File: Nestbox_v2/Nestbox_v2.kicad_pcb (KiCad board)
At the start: 2 copper layers, 85 x 60 mm, 108 parts, among them CON301 Micro_SD_Card, J201 BATT_CONN_01X02, J401 LB_DETECT_CONN_01X04, J402 CONN_01X05, J501 CONN_01X01, J502 CONN_01X06, J601 LOAD_CELL_CONN_01X04, J701 RFID_CONN_01X05, P301 RX/TX, P302 TST/RST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

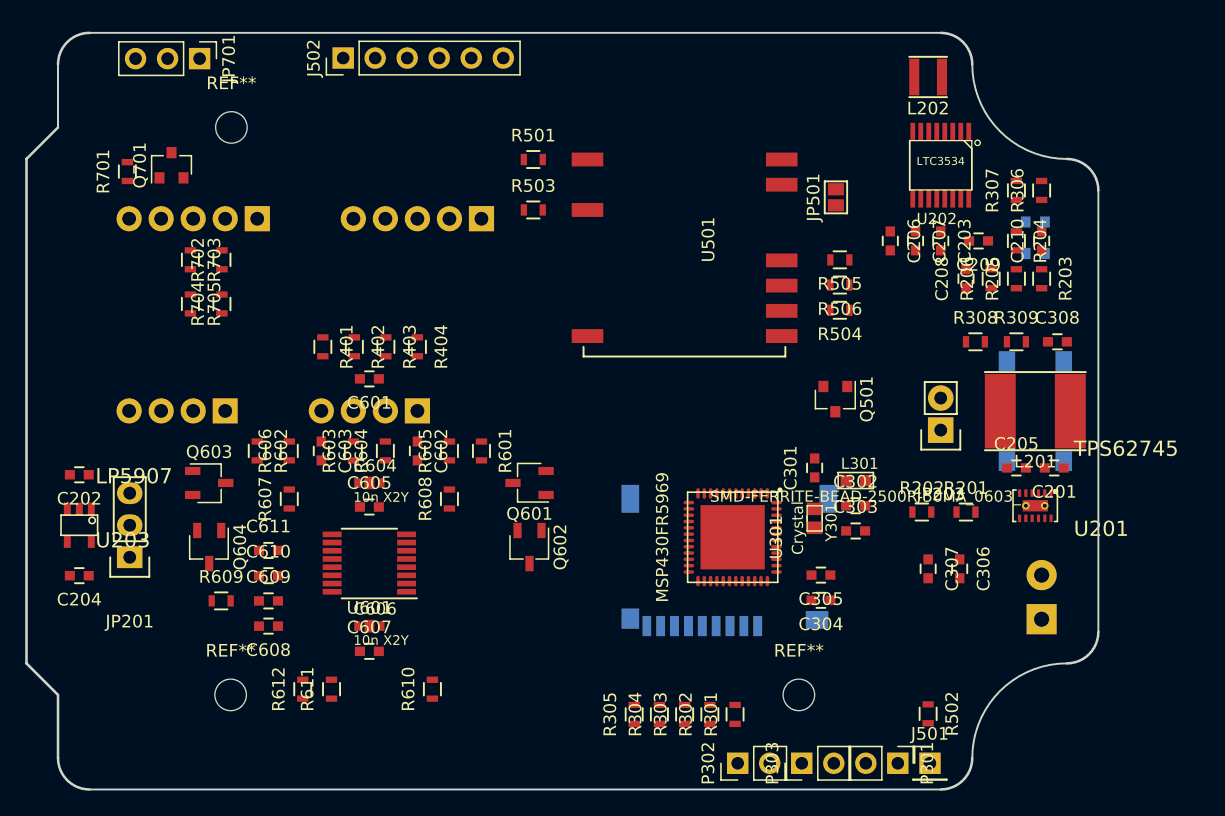
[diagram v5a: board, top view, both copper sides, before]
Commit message: routed all tracks except ground plane
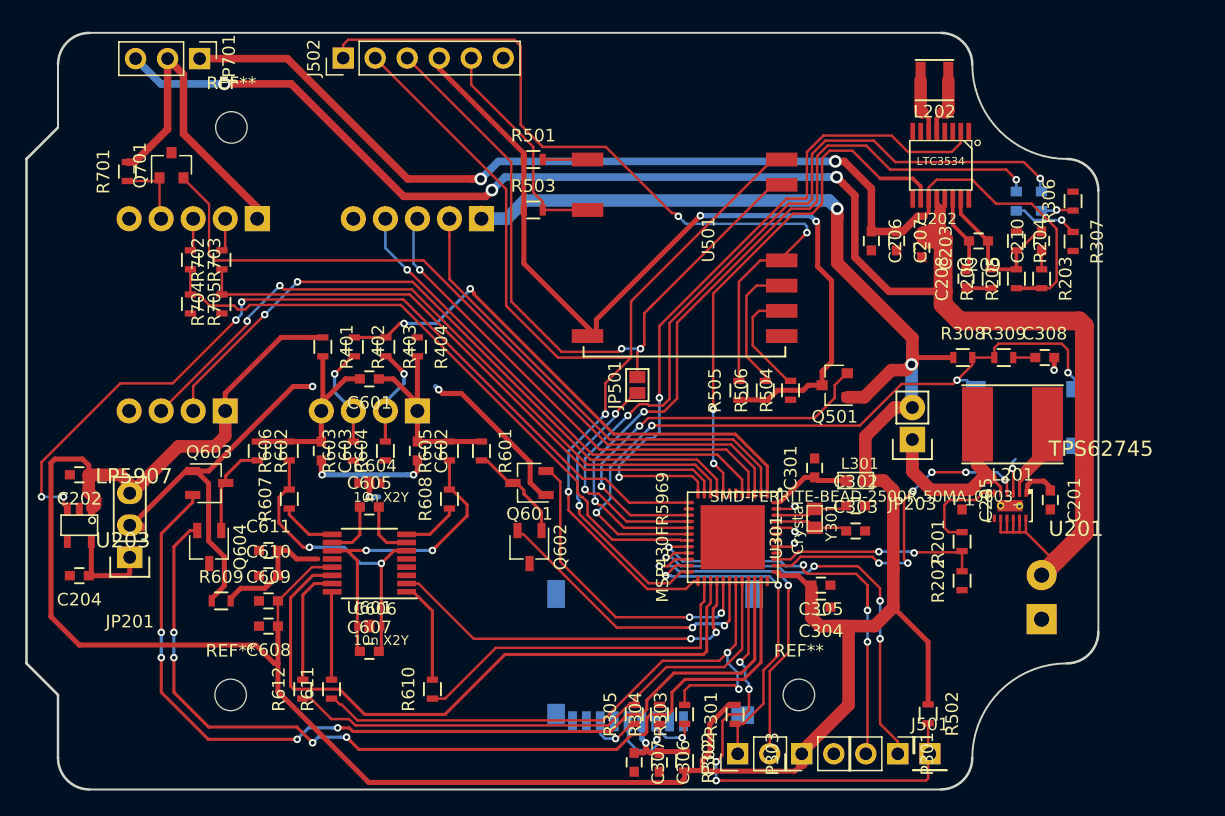
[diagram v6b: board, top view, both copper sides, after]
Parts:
- moved C306 28.3 mm to (82.7, 185.3)
- moved C307 27.9 mm to (80.7, 185.3)
- moved JP501 21.7 mm to (80.9, 155.4)
- moved R505 13.1 mm to (89.0, 155.9), turned to 90 degrees
- moved R506 10.2 mm to (91.1, 155.9), turned to 90 degrees
- moved CON301 9.58 mm to (82.3, 182.1)
- moved R504 7.45 mm to (93.1, 155.8), turned to 90 degrees
- moved R202 6.31 mm to (106.7, 170.9), turned to 90 degrees
- moved R307 6.04 mm to (115.5, 144.0), turned to 270 degrees
- moved C205 5.01 mm to (106.7, 164.5), turned to 270 degrees
- moved D302 4.42 mm to (111.0, 140.8), turned to 270 degrees
- moved R302 4.21 mm to (84.7, 185.2), turned to 270 degrees
- moved R306 2.63 mm to (115.5, 140.8)
- moved C201 2.56 mm to (113.7, 164.5), turned to 270 degrees
- moved JP203 2.37 mm to (102.8, 159.8)
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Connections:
- U201 pad 2: (no net) -> Net-(L201-Pad1)
- U201 pad 3: Net-(L201-Pad1) -> GND
- U301 pad 11: (no net) -> /Control/RFID_CLK
- U301 pad 14: /Control/BAT_TEST_ENABLE -> (no net)
- U301 pad 38: /PIR_OUT1 -> /Control/BAT_TEST_ENABLE
- U301 pad 39: /PIR_OUT2 -> /Control/HK_BAT_V
- U301 pad 4: (no net) -> /PIR_OUT1
- U301 pad 40: /Control/RFID_CLK -> (no net)
- U301 pad 5: (no net) -> /PIR_OUT2
- U301 pad 6: /Control/HK_BAT_V -> (no net)
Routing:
- net +3V3: track 0.00 -> 246.2 mm, vias 0 -> 2
- net +BATT: track 0.00 -> 144.1 mm, vias 0 -> 3
- net +5V: track 0.00 -> 88.8 mm, vias 0 -> 2
- net /Communication/ESP12_TX: track 0.00 -> 83.2 mm, vias 0 -> 2
- net /Load_Cell/EXC_B_P: track 0.00 -> 74.8 mm, vias 0 -> 4
- net /Load_Cell/EXC_B_N: track 0.00 -> 73.5 mm, vias 0 -> 4
- net /Communication/ESP12_VCC: track 0.00 -> 70.4 mm, vias 0 -> 2
- net /Power/LDO_EN: track 0.00 -> 69.5 mm, vias 0 -> 4
- net /Control/DBG_LED1: track 0.00 -> 66.3 mm, vias 0 -> 3
- net /Communication/DTR: track 0.00 -> 63.2 mm, vias 0 -> 2
- net /Control/DBG_LED2: track 0.00 -> 63.1 mm, vias 0 -> 3
- net /Control/RFID_SLEEP_N: track 0.00 -> 59.2 mm
- net /Control/DBG_Switch: track 0.00 -> 58.6 mm, vias 0 -> 4
- net /Passage Detector/LB2_DETECT: track 0.00 -> 55.4 mm, vias 0 -> 2
- net /Control/5V_ENABLE: track 0.00 -> 55.0 mm, vias 0 -> 2
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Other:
- net class Analog added: clearance 0.25, trace_width 0.25, via_dia 0.7, via_drill 0.4
- net class Default: trace_width 0.25 -> 0.2; via_drill 0.4 -> 0.3
- net class Power added: clearance 0.25, trace_width 0.4, via_dia 1, via_drill 0.6

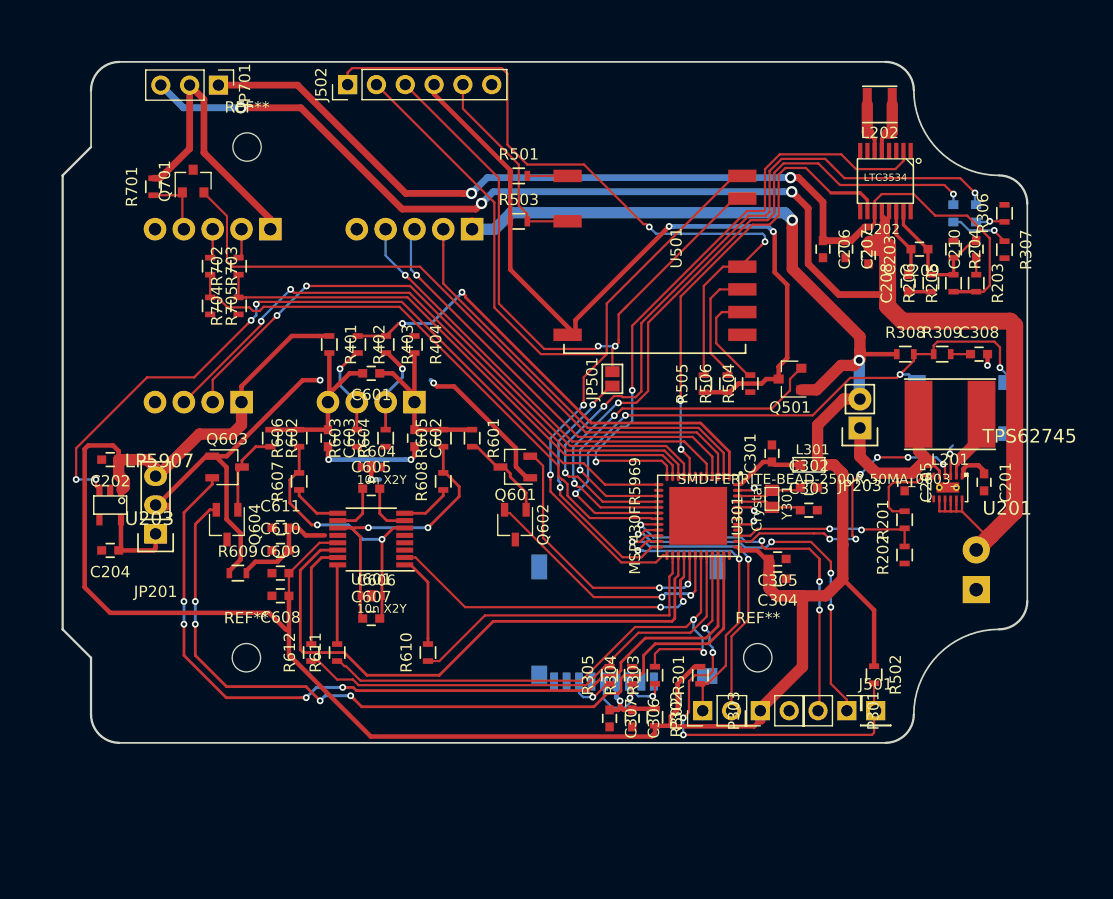
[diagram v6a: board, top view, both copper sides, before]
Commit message: added stitching vias at power stage; reverse polarity protection and SD car enable mosfet
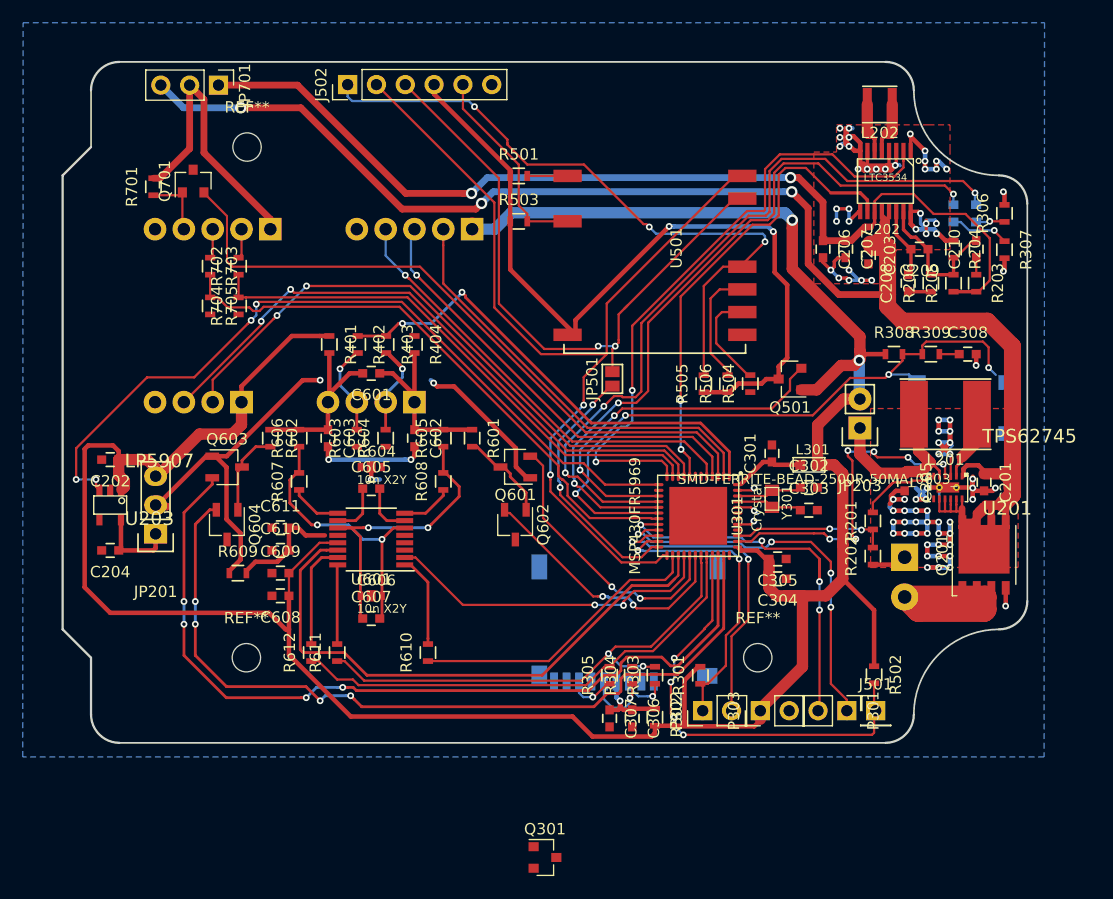
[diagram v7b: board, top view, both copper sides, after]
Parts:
- added Q201: Q_PMOS_DGS, Octanis3:TDSON-8-1_HandSoldering, F.Cu at (113.7, 170.9)
- added Q301: NTR3A052PZT1G, TO_SOT_Packages_SMD:SOT-23, F.Cu at (75.0, 197.6)
- moved J201 6.93 mm to (106.7, 171.1), turned to 270 degrees
- moved R201 2.80 mm to (103.9, 167.9)
- moved R202 2.80 mm to (103.9, 171.0)
- moved C308 1.00 mm to (112.2, 153.2)
- moved R308 1.00 mm to (105.8, 153.2)
- moved R309 1.00 mm to (109.0, 153.2)
- moved L201 0.40 mm to (110.3, 158.5)
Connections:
- J201 pad 2: +BATT -> /Power/batt_in
- R302 pad 2: +3V3 -> Net-(Q301-Pad3)
- U201 pad EXPA: (no net) -> GND
- U201 pad GND1: (no net) -> GND
- U201 pad GND2: (no net) -> GND
- U301 pad 14: (no net) -> /Control/SD_CARD_ENABLE
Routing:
- net GND: track 15.7 -> 135.2 mm, vias 5 -> 83
- net /Power/batt_in: track 0.00 -> 15.8 mm
- net +BATT: track 144.1 -> 152.3 mm
- net /Control/SPI_MOSI: track 49.3 -> 44.1 mm
- net /Communication/DTR: track 63.2 -> 58.6 mm, vias 2 -> 3
- net /Control/LOADCELL_SPI_CS: track 33.1 -> 29.5 mm
- net /Control/BAT_TEST_ENABLE: track 26.3 -> 29.1 mm
- net /Control/HK_BAT_V: track 16.6 -> 13.8 mm
- net /Load_Cell/DRDY_N: track 52.7 -> 50.7 mm
- net /Control/SPI_CLK: track 28.4 -> 26.3 mm
- net Net-(Q301-Pad3): track 0.00 -> 2.05 mm
- net +3V3: track 246.2 -> 244.2 mm
- net /Control/SPI_MISO: track 43.9 -> 42.6 mm
- net /Control/5V_ENABLE: track 55.0 -> 55.9 mm
- net /Load_Cell/EXC_B_N: track 73.5 -> 72.7 mm
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- added copper zone on B.Cu, net GND
- added copper zone on F.Cu, net GND

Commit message: finished routing. DRC clean
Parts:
- removed R302: 0E, Resistors_SMD:R_0603
- CON301: footprint SeeedOPL-Connector-2016:MICRO-SD9+4P-SMD-16.1X14.5X1.85MM -> Octanis3:MICRO-SD9+4P-SMD-16.1X14.5X1.85MM
- moved Q301 12.7 mm to (76.7, 185.0), turned to 180 degrees
- moved Q601 7.16 mm to (69.4, 169.7)
- moved Q602 7.16 mm to (69.4, 174.8)
- moved R303 3.00 mm to (81.7, 181.5)
- moved R304 3.00 mm to (79.7, 181.5)
- moved R305 3.00 mm to (77.7, 181.5)
- moved C306 1.04 mm to (81.7, 185.0)
- moved C307 1.04 mm to (79.7, 185.0)
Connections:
- CON301 pad 9: (no net) -> GND
- Q301 pad 3: Net-(Q301-Pad3) -> Net-(C306-Pad1)
- R304 pad 2: (no net) -> /Control/SPI_CLK
- U301 pad 41: GNDA -> GND
- U301 pad 44: GNDA -> GND
- U301 pad 47: GNDA -> GND
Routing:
- net GND: track 135.2 -> 225.6 mm, vias 83 -> 111
- net /Control/SD_CARD_ENABLE: track 0.00 -> 36.6 mm, vias 0 -> 4
- net Net-(Q601-Pad3): track 8.11 -> 16.0 mm
- net Net-(C205-Pad1): track 17.9 -> 24.7 mm
- net GNDA: track 5.44 -> 0.00 mm, vias 3 -> 0
- net /Control/SPI_CLK: track 26.3 -> 31.6 mm, vias 0 -> 2
- net /Control/LORA_RESET_N: track 39.1 -> 43.5 mm, vias 4 -> 2
- net Net-(CON301-Pad5): track 6.10 -> 2.11 mm
- net /Load_Cell/AIN2: track 4.65 -> 8.56 mm
- net /Load_Cell/AIN1: track 4.65 -> 8.56 mm
- net +BATT: track 152.3 -> 156.0 mm
- net /Power/batt_in: track 15.8 -> 18.9 mm
- net /Load_Cell/EXC_B_P: track 75.4 -> 78.1 mm, vias 4 -> 6
- net /Load_Cell/EXC_B_N: track 72.7 -> 75.3 mm, vias 4 -> 6
- net /Control/SPI_MOSI: track 44.1 -> 41.7 mm, vias 2 -> 0
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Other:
- net class Analog: clearance 0.25 -> 0.2
